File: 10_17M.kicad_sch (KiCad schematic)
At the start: 7 parts

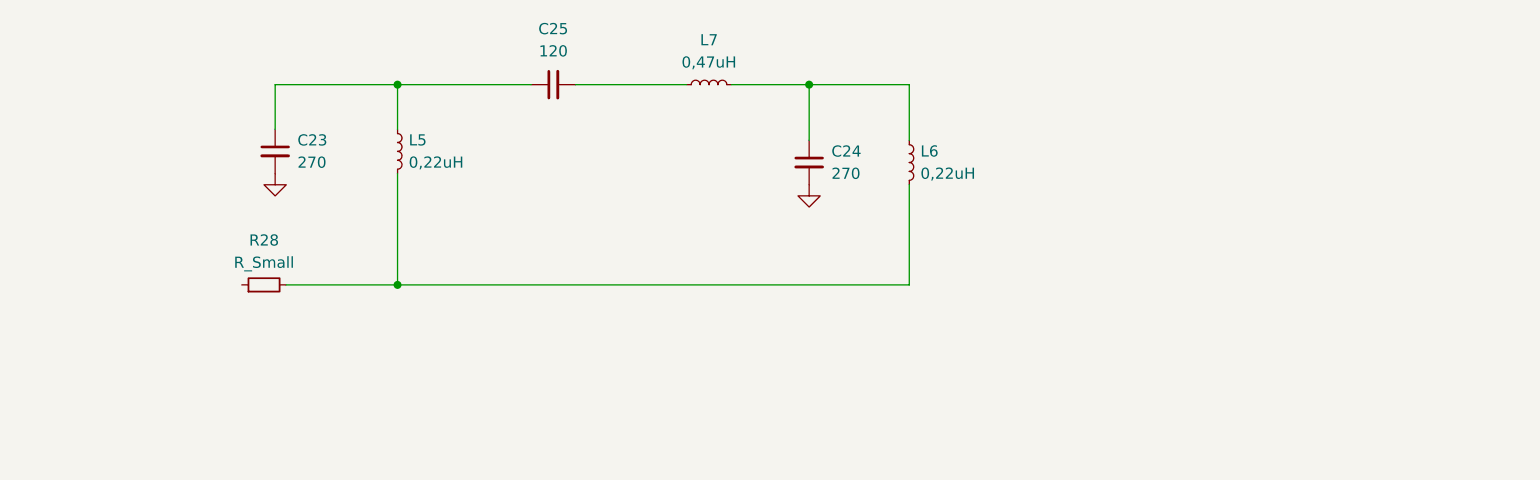
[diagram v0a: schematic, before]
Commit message: 10_17M BPF done
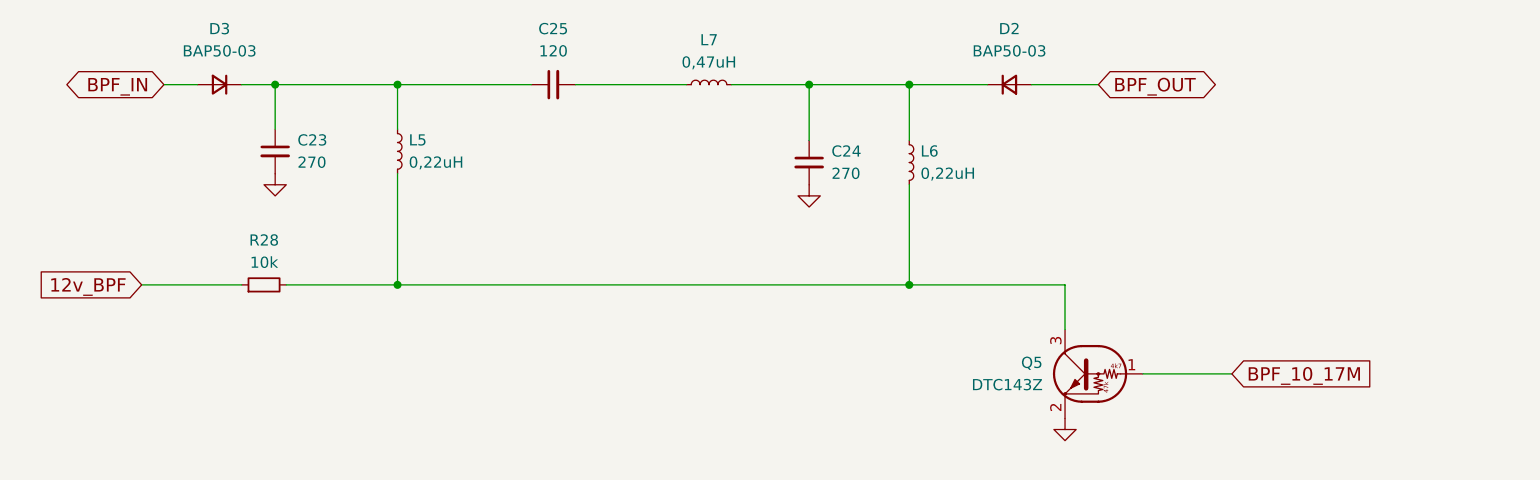
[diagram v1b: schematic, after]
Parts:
- added D2, D3: BAP50-03, Diode_SMD:D_SOD-323_HandSoldering, symbol Device:D_Small
- added Q5: DTC143Z, Package_TO_SOT_SMD:SOT-523, symbol Transistor_BJT:DTC143Z
- C23, C24: footprint (none) -> Capacitor_SMD:C_0603_1608Metric_Pad1.08x0.95mm_HandSolder; JLCPCB (none) -> C694496
- C25: footprint (none) -> Capacitor_SMD:C_0603_1608Metric_Pad1.08x0.95mm_HandSolder; JLCPCB (none) -> C599667
- L5, L6: footprint (none) -> Inductor_SMD:L_1210_3225Metric_Pad1.42x2.65mm_HandSolder; JLCPCB (none) -> C89026
- L7: footprint (none) -> Inductor_SMD:L_1210_3225Metric_Pad1.42x2.65mm_HandSolder; JLCPCB (none) -> C89029
- R28: value R_Small -> 10k; footprint (none) -> Resistor_SMD:R_0603_1608Metric_Pad0.98x0.95mm_HandSolder; JLCPCB (none) -> C25804
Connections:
- net GND: now also Q5.2 (E)
- net at C24.1, L6.1, L7.2: now also D2.1 (K)
- net at C23.1, C25.1, L5.1: now also D3.1 (K)
- net 12v_BPF: now reaches R28.1
- net at L5.2, L6.2, R28.2: now also Q5.3 (C)
- new net BPF_10_17M: Q5.1 (B)
- new net BPF_IN: D3.2 (A)
- new net BPF_OUT: D2.2 (A)

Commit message: add custom footprints, progress on schema and PCB
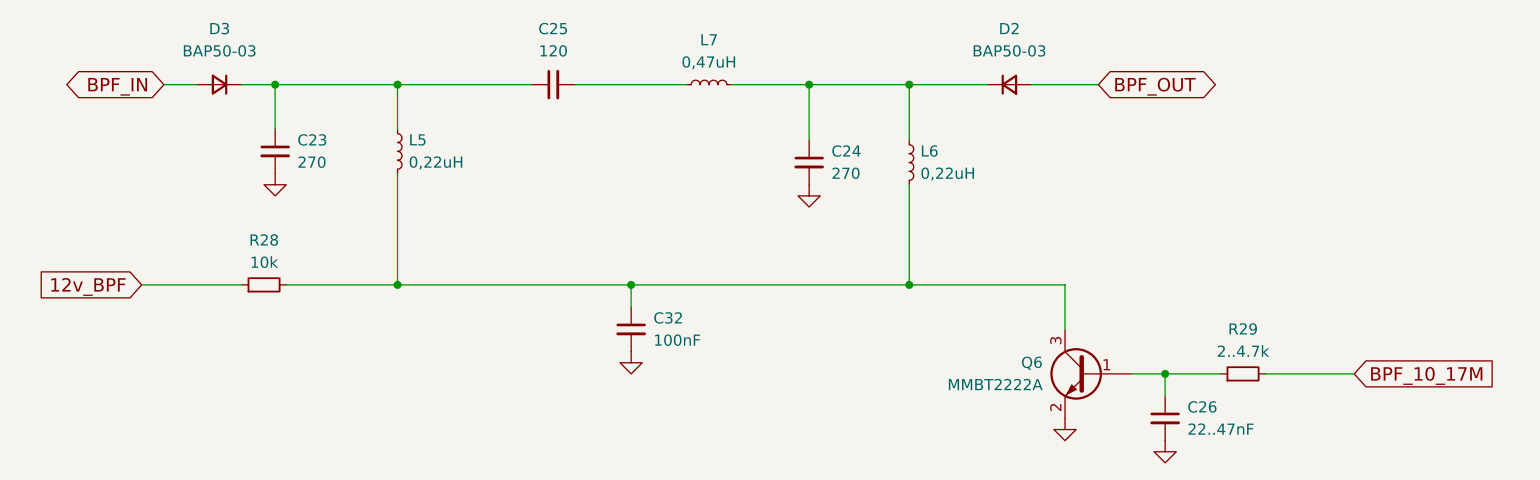
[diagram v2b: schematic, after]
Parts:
- removed Q5: DTC143Z, Package_TO_SOT_SMD:SOT-523, symbol Transistor_BJT:DTC143Z
- added C26: 22..47nF, SDR_footprints:C_1206_0603, symbol Device:C_Small
- added C32: 100nF, SDR_footprints:C_1206_0603, symbol Device:C_Small
- added Q6: MMBT2222A, Package_TO_SOT_SMD:SOT-23, symbol Transistor_BJT:MMBT2222A
- added R29: 2..4.7k, SDR_footprints:R_1206_0603, symbol Device:R_Small
- C23, C24, C25: footprint Capacitor_SMD:C_0603_1608Metric_Pad1.08x0.95mm_HandSolder -> SDR_footprints:C_1206_0603
- L5, L6: footprint Inductor_SMD:L_1210_3225Metric_Pad1.42x2.65mm_HandSolder -> SDR_footprints:Resistor_SMD+THTuniversal_0603to2512_RM10_HandSoldering; JLCPCB C89026 -> (none)
- L7: footprint Inductor_SMD:L_1210_3225Metric_Pad1.42x2.65mm_HandSolder -> SDR_footprints:Resistor_SMD+THTuniversal_0603to2512_RM10_HandSoldering; JLCPCB C89029 -> (none)
- R28: footprint Resistor_SMD:R_0603_1608Metric_Pad0.98x0.95mm_HandSolder -> SDR_footprints:R_1206_0603
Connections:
- net BPF_10_17M: now also R29.2
- net GND: now also C26.2, C32.2, Q6.2 (E)
- net at L5.2, L6.2, R28.2: now also C32.1, Q6.3 (C)
- new net: C26.1, Q6.1 (B), R29.1

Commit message: progress on PCB
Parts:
- R28: footprint SDR_footprints:R_1206_0603 -> Resistor_SMD:R_0603_1608Metric_Pad0.98x0.95mm_HandSolder
